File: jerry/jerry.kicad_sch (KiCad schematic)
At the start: 35 parts, among them J1 0532610471, J2 0532610471, J3 0532610471, J4 XT60-M, J7 TSW-106-06-F-S-LL, J8 TSW-106-06-F-S-LL, U1 RASPBERRY_PI_4B_4GB, U2 A4988_STEPPER_MOTOR_DRIVER_CA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, U3 LM338T, U4 LM338T

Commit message: Finished PCB
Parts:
- C1, C2, C3, C4, C5: footprint (none) -> Capacitor_SMD:C_0201_0603Metric_Pad0.64x0.40mm_HandSolder
- F1: footprint (none) -> jerry:FUSC3215X83N
- R1, R10, R11, R2, R3, R4, R5, R6, R7, R8, R9: footprint (none) -> Resistor_SMD:R_0201_0603Metric_Pad0.64x0.40mm_HandSolder
- U2: footprint (none) -> jerry:MODULE_A4988_STEPPER_MOTOR_DRIVER_CARRIER
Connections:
- net +5V: now also U1.2 (5V), U1.4 (5V)
- net GND: now also J7.06, J8.06, U1.14 (GND), U1.20 (GND), U1.25 (GND), U1.30 (GND), U1.34 (GND), U1.39 (GND), U1.6 (GND), U1.9 (GND), U2.8 (GND), U2.9 (GND)
- net LEDInd1: now also U1.3 (GPIO2/SDA1)
- net LEDInd2: now also U1.5 (GPIO3/SCL1)
- net LEDInd3: now also U1.11 (GPIO17/GPIO_GEN0)
- net M1A: now also U2.16 (OUT1)
- net M1B: now also U2.14 (OUT3)
- net M2A: now also U2.15 (OUT2)
- net M2B: now also U2.13 (OUT4)
- net TFMINIRX1: now also U1.8 (GPIO14/TXD0)
- net TFMINIRX2: now also U1.7 (GPIO4/GPIO_GCKL)
- net TFMINIRX3: now also U1.32 (GPIO12)
- net TFMINITX1: now also U1.10 (GPIO15/RXD0)
- net TFMINITX2: now also U1.29 (GPIO5)
- net TFMINITX3: now also U1.33 (GPIO13)
- net IN1: now reaches U2.4 (IN1)
- net IN1: now also U1.13 (GPIO27/GPIO_GEN2)
- net IN2: now reaches U2.5 (IN2)
- net IN2: now also U1.15 (GPIO22/GPIO_GEN3)
- net IN3: now reaches U2.6 (IN3)
- net IN3: now also U1.19 (GPIO10/SPI_MOSI)
- net IN4: now reaches U2.7 (IN4)
- net IN4: now also U1.21 (GPIO9/SPI_MISO)
- net OUTA_A: now reaches J7.04
- net OUTA_A: now also U1.35 (GPIO19)
- net OUTB_A: now reaches J7.05
- net OUTB_A: now also U1.37 (GPIO26)
- net OUTA_B: now reaches U1.27 (ID_SD)
- net OUTA_B: now also J8.04
- net OUTB_B: now reaches U1.31 (GPIO6)
- net OUTB_B: now also J8.05

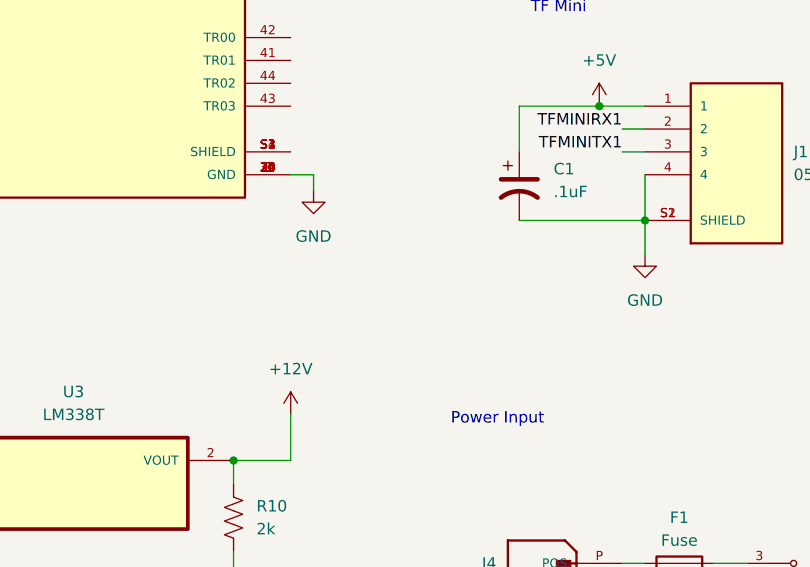
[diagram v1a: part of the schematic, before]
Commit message: Updated for manufacturing
fixed gerber errors, genereated gerbers
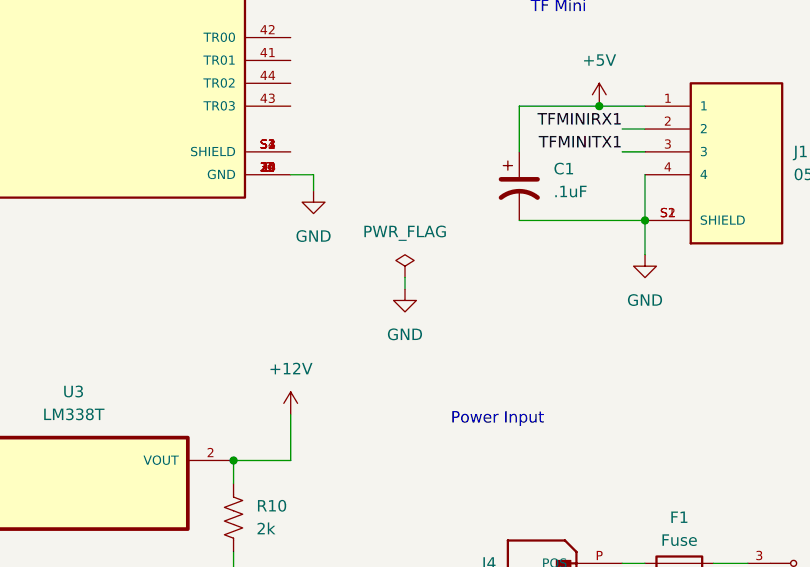
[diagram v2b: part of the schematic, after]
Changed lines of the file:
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@@
+    (stroke (width 0) (type default))
+  )
+  (wire (pts (xy 86.36 99.06) (xy 86.36 100.33))
     (stroke (width 0) (type default))
   )
@@
     )
   )
+  (symbol (lib_id "power:GND") (at 86.36 100.33 0) (unit 1)
+    (in_bom yes) (on_board yes) (dnp no) (fields_autoplaced)
+    (property "Reference" "#PWR033" (at 86.36 106.68 0)
+      (effects (font (size 1.27 1.27)) hide)
+    )
+    (property "Value" "GND" (at 86.36 105.41 0)
+      (effects (font (size 1.27 1.27)))
+    )
+    (property "Footprint" "" (at 86.36 100.33 0)
+      (effects (font (size 1.27 1.27)) hide)
+    )
+    (property "Datasheet" "" (at 86.36 100.33 0)
+      (effects (font (size 1.27 1.27)) hide)
+    )
+    (pin "1")
+    (instances
+      (project "jerry"
+        (path "/abc7eadc-e8ed-4c2d-abd9-433deb234b37"
+          (reference "#PWR033") (unit 1)
+        )
+      )
+    )
+  )
   (symbol (lib_id "jerry:LM338T") (at 49.53 121.92 0) (unit 1)
     (in_bom yes) (on_board yes) (dnp no) (fields_autoplaced)
@@
         )
       )
+    )
+  )
+  (symbol (lib_id "power:PWR_FLAG") (at 86.36 99.06 0) (unit 1)
+    (in_bom yes) (on_board yes) (dnp no) (fields_autoplaced)
+    (property "Reference" "#FLG01" (at 86.36 97.155 0)
+      (effects (font (size 1.27 1.27)) hide)
+    )
+    (property "Value" "PWR_FLAG" (at 86.36 93.98 0)
+      (effects (font (size 1.27 1.27)))
+    )
+    (property "Footprint" "" (at 86.36 99.06 0)
+      (effects (font (size 1.27 1.27)) hide)
+    )
+    (property "Datasheet" "~" (at 86.36 99.06 0)
+      (effects (font (size 1.27 1.27)) hide)
+    )
+    (pin "1")
+    (instances
+      (project "jerry"
+        (path "/abc7eadc-e8ed-4c2d-abd9-433deb234b37"
+          (reference "#FLG01") (unit 1)
+        )
+      )
